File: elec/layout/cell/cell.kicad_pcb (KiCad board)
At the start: 4 copper layers, 65 parts

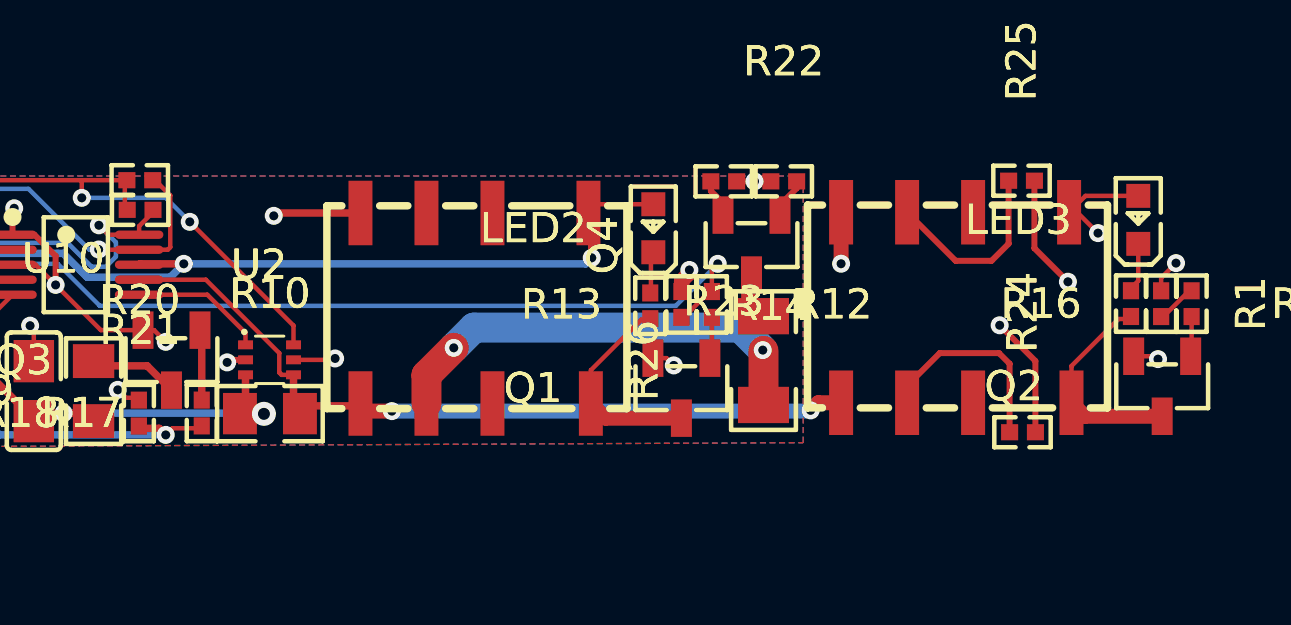
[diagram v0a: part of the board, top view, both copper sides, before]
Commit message: swap to relay with 20k in stock, through hole not smt
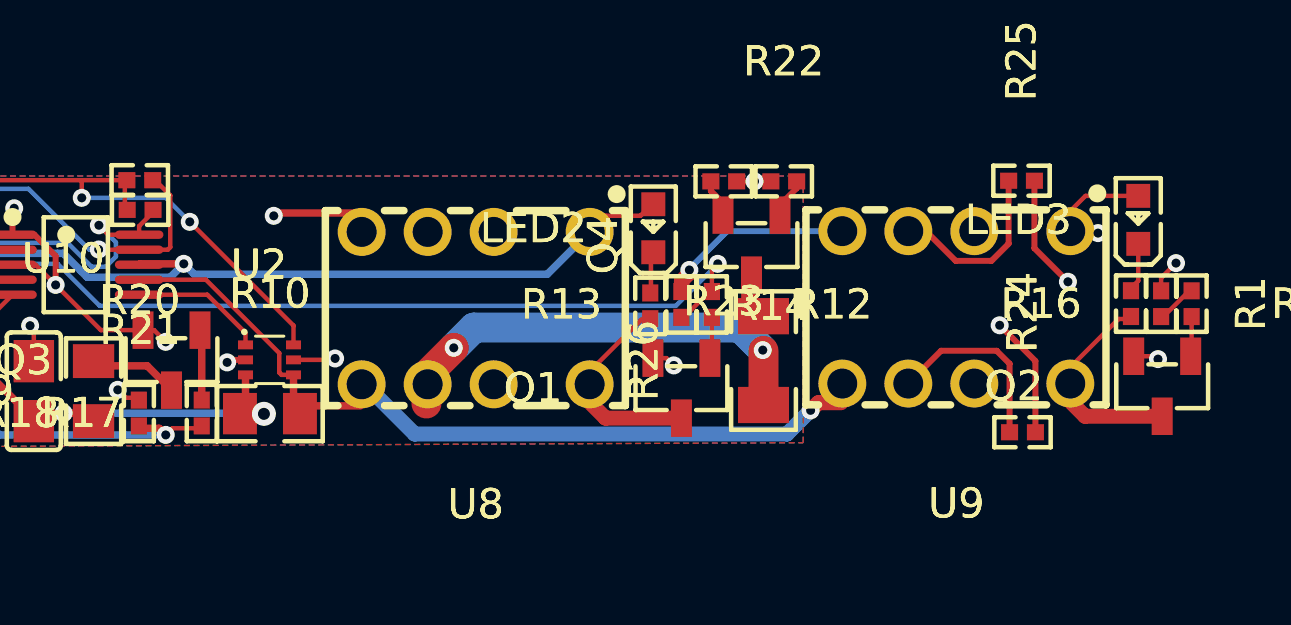
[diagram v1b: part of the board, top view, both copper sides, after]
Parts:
- U8, U9: footprint lib:RELAY-SMD_HFD4-5-SR -> atopile:RELAY-TH_HFDXXX-689a1e
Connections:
- C1 pad 1: hv-1 -> hv-10
- C1 pad 2: gnd-2 -> gnd
- C10 pad 1: hv-10 -> hv-6
- C10 pad 2: gnd -> gnd-8
- C11 pad 1: hv-10 -> hv-6
- C11 pad 2: gnd -> gnd-8
- C12 pad 1: hv-9 -> hv-7
- C12 pad 2: gnd -> gnd-8
- C13 pad 1: hv-4 -> hv-5
- C13 pad 2: gnd-7 -> gnd-4
- C14 pad 1: hv-4 -> hv-5
- C14 pad 2: gnd-7 -> gnd-4
- C15 pad 1: hv -> hv-9
- C15 pad 2: gnd -> gnd-8
- C16 pad 1: hv-6 -> hv-1
- C16 pad 2: gnd -> gnd-8
- C2 pad 1: hv -> hv-9
- C2 pad 2: gnd -> gnd-8
- C3 pad 1: hv -> hv-9
- C3 pad 2: gnd -> gnd-8
- C4 pad 1: hv -> hv-9
- C4 pad 2: gnd -> gnd-8
- C5 pad 1: hv -> hv-9
- C5 pad 2: gnd -> gnd-8
- C6 pad 1: hv-7 -> hv-4
- C6 pad 2: gnd -> gnd-8
- C7 pad 1: hv-7 -> hv-4
- C7 pad 2: gnd -> gnd-8
- C8 pad 1: hv-7 -> hv-4
- C8 pad 2: gnd -> gnd-8
- L1 pad 2: hv-7 -> hv-4
- L2 pad 1: hv-10 -> hv-6
- L2 pad 2: hv-9 -> hv-7
- LED1 pad 2: hv -> hv-9
- LED2 pad 2: hv -> hv-9
- LED3 pad 2: hv-4 -> hv-5
- Q1 pad 2: gnd -> gnd-8
- Q2 pad 2: gnd-7 -> gnd-4
- Q3 pad 2: gnd -> gnd-8
- Q3 pad 3: gnd-8 -> gnd-1
- Q4 pad 2: gnd-3 -> gnd-7
- Q4 pad 3: gnd-4 -> gnd-2
- R10 pad 1: hv-9 -> hv-7
- R10 pad 2: line-3 -> line-7
- R11 pad 2: gnd -> gnd-8
- R12 pad 1: line -> line-2
- R13 pad 1: line -> line-2
- R13 pad 2: gnd -> gnd-8
- R15 pad 1: line-7 -> line-11
- R16 pad 1: line-7 -> line-11
- R16 pad 2: gnd-7 -> gnd-4
- R17 pad 1: line-5 -> line-3
- R18 pad 1: line-5 -> line-3
- R18 pad 2: gnd -> gnd-8
- R19 pad 1: hv-9 -> hv-7
- R19 pad 2: gnd-8 -> gnd-1
- R20 pad 1: line-8 -> line
- R20 pad 2: hv-6 -> hv-1
- R21 pad 1: line-11 -> line-8
- R21 pad 2: hv-6 -> hv-1
- R22 pad 1: line-4 -> line-10
- R23 pad 1: line-4 -> line-10
- R23 pad 2: gnd-3 -> gnd-7
- R24 pad 1: hv-5 -> hv
- R24 pad 2: hv-3 -> hv-2
- R25 pad 1: gnd-6 -> gnd-5
- R25 pad 2: gnd-5 -> gnd-6
- R26 pad 2: gnd-4 -> gnd-2
- R3 pad 1: hv-7 -> hv-4
- R4 pad 2: gnd -> gnd-8
- R5 pad 1: line-14 -> line-1
- R7 pad 1: hv-10 -> hv-6
- R8 pad 2: gnd -> gnd-8
- R9 pad 1: line-2 -> line-6
- U1 pad 1: hv-1 -> hv-10
- U1 pad 2: gnd-2 -> gnd
- U1 pad 4: gnd -> gnd-8
- U1 pad 6: hv -> hv-9
- U10 pad 1: hv-6 -> hv-1
- U10 pad 10: gpio-net-1 -> gpio-net-2
- U10 pad 12: line-11 -> line-8
- U10 pad 13: line-8 -> line
- U10 pad 14: hv-6 -> hv-1
- U10 pad 15: hv-6 -> hv-1
- U10 pad 16: gnd -> gnd-8
- U10 pad 17: gnd -> gnd-8
- U10 pad 2: gpio-net-2 -> gpio-net-1
- U10 pad 4: line-14 -> line-1
- U10 pad 5: line-2 -> line-6
- U10 pad 6: gnd -> gnd-8
- U10 pad 7: line-5 -> line-3
- U10 pad 8: line -> line-2
- U10 pad 9: line-4 -> line-10
- U11 pad 1: hv-2 -> hv-3
- U11 pad 2: line-13 -> line-9
- U11 pad 3: line-12 -> line-13
- U11 pad 4: gnd-1 -> gnd-3
- U11 pad 5: gnd -> gnd-8
- U11 pad 6: line-11 -> line-8
- U11 pad 7: line-8 -> line
- U11 pad 8: hv-6 -> hv-1
- U12 pad 1: hv-4 -> hv-5
- U12 pad 2: line-10 -> line-14
- U12 pad 3: gnd-7 -> gnd-4
- U12 pad 4: line-6 -> line-4
- U13 pad 1: hv-4 -> hv-5
- U13 pad 2: line-6 -> line-4
- U13 pad 3: gnd-7 -> gnd-4
- U13 pad 4: line-1 -> line-5
- U14 pad 1: gnd -> gnd-8
- U14 pad 2: hv-6 -> hv-1
- U14 pad 3: hv -> hv-9
- U2 pad 1: gnd -> gnd-8
- U2 pad 10: line-11 -> line-8
- U2 pad 3: gnd -> gnd-8
- U2 pad 4: hv-7 -> hv-4
- U2 pad 5: hv-10 -> hv-6
- U2 pad 6: line-9 -> line-12
- U2 pad 7: line-3 -> line-7
- U2 pad 8: hv -> hv-9
- U2 pad 9: line-8 -> line
- U3 pad 2: gnd -> gnd-8
- U3 pad 3: hv-6 -> hv-1
- U3 pad 4: line-8 -> line
- U3 pad 5: line-11 -> line-8
- U3 pad 6: hv -> hv-9
- U4 pad 1: gnd -> gnd-8
- U4 pad 3: hv -> hv-9
- U5 pad 2: gnd -> gnd-8
- U5 pad 3: hv-6 -> hv-1
- U5 pad 4: line-8 -> line
- U5 pad 5: line-11 -> line-8
- U5 pad 6: gnd -> gnd-8
- U6 pad 1: hv-10 -> hv-6
- U6 pad 3: gnd -> gnd-8
- U6 pad 6: hv-7 -> hv-4
- U6 pad 7: gnd -> gnd-8
- U7 pad 1: line-9 -> line-12
- U7 pad 2: gnd -> gnd-8
- U7 pad 3: hv-9 -> hv-7
- U7 pad 4: line-3 -> line-7
- U7 pad 5: gnd -> gnd-8
- U7 pad 6: hv-6 -> hv-1
- U8 pad 1: hv -> hv-9
- U8 pad 2: (no net) -> output_relay.relay.footprint.pins[1].net-net
- U8 pad 3: gnd-3 -> gnd-7
- U8 pad 4: gnd -> gnd-8
- U8 pad 5: line-3 -> line-7
- U8 pad 7: (no net) -> output_relay.relay.footprint.pins[6].net-net
- U9 pad 1: hv-4 -> hv-5
- U9 pad 2: (no net) -> dmm_relay.relay.footprint.pins[1].net-net
- U9 pad 3: gnd-6 -> gnd-5
- U9 pad 4: gnd -> gnd-8
- U9 pad 5: line-3 -> line-7
- U9 pad 6: hv-5 -> hv
- U9 pad 7: (no net) -> dmm_relay.relay.footprint.pins[6].net-net
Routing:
- net gnd-8: track 3.42 -> 110.0 mm, vias 0 -> 31
- net gnd: track 106.1 -> 10.8 mm, vias 32 -> 1
- net hv: track 75.3 -> 6.35 mm, vias 4 -> 0
- net hv-9: track 13.2 -> 74.7 mm, vias 2 -> 3
- net line-11: track 43.5 -> 1.44 mm, vias 5 -> 0
- net line-10: track 0.00 -> 30.5 mm, vias 0 -> 2
- net hv-1: track 4.33 -> 34.0 mm, vias 0 -> 8
- net line-4: track 30.5 -> 2.29 mm, vias 2 -> 0
- net line-7: track 1.44 -> 27.5 mm, vias 0 -> 1
- net line-2: track 7.72 -> 30.4 mm
- net hv-6: track 34.0 -> 15.6 mm, vias 8 -> 0
- net line: track 30.4 -> 44.5 mm, vias 2 -> 4
- net line-5: track 13.5 -> 0.00 mm, vias 2 -> 0
- net line-3: track 26.6 -> 13.5 mm
- net line-14: track 12.8 -> 0.00 mm, vias 2 -> 0
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- added copper zone on B.Cu, net gnd-8
- added copper zone on F.Cu, net gnd-8
- added copper zone on In2.Cu, net gnd-8
- added copper zone on In1.Cu, net hv-1
- removed copper zone on B.Cu, net gnd
- removed copper zone on F.Cu, net gnd
- removed copper zone on In2.Cu, net gnd
- removed copper zone on In1.Cu, net hv-6

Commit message: Cleanup layout
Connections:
- C1 pad 1: hv-10 -> hv-9
- C10 pad 1: hv-6 -> hv-4
- C10 pad 2: gnd-8 -> gnd-7
- C11 pad 1: hv-6 -> hv-4
- C11 pad 2: gnd-8 -> gnd-7
- C12 pad 1: hv-7 -> hv-1
- C12 pad 2: gnd-8 -> gnd-7
- C13 pad 1: hv-5 -> hv-7
- C13 pad 2: gnd-4 -> gnd-1
- C14 pad 1: hv-5 -> hv-7
- C14 pad 2: gnd-4 -> gnd-1
- C15 pad 1: hv-9 -> hv-3
- C15 pad 2: gnd-8 -> gnd-7
- C16 pad 1: hv-1 -> hv-5
- C16 pad 2: gnd-8 -> gnd-7
- C2 pad 1: hv-9 -> hv-3
- C2 pad 2: gnd-8 -> gnd-7
- C3 pad 1: hv-9 -> hv-3
- C3 pad 2: gnd-8 -> gnd-7
- C4 pad 1: hv-9 -> hv-3
- C4 pad 2: gnd-8 -> gnd-7
- C5 pad 1: hv-9 -> hv-3
- C5 pad 2: gnd-8 -> gnd-7
- C6 pad 1: hv-4 -> hv-10
- C6 pad 2: gnd-8 -> gnd-7
- C7 pad 1: hv-4 -> hv-10
- C7 pad 2: gnd-8 -> gnd-7
- C8 pad 1: hv-4 -> hv-10
- C8 pad 2: gnd-8 -> gnd-7
- L1 pad 2: hv-4 -> hv-10
- L2 pad 1: hv-6 -> hv-4
- L2 pad 2: hv-7 -> hv-1
- LED1 pad 2: hv-9 -> hv-3
- LED2 pad 2: hv-9 -> hv-3
- LED3 pad 2: hv-5 -> hv-7
- Q1 pad 2: gnd-8 -> gnd-7
- Q2 pad 2: gnd-4 -> gnd-1
- Q3 pad 2: gnd-8 -> gnd-7
- Q3 pad 3: gnd-1 -> gnd-4
- Q4 pad 2: gnd-7 -> gnd-6
- Q4 pad 3: gnd-2 -> gnd-3
- R10 pad 1: hv-7 -> hv-1
- R10 pad 2: line-7 -> line-10
- R11 pad 2: gnd-8 -> gnd-7
- R12 pad 1: line-2 -> line-12
- R13 pad 1: line-2 -> line-12
- R13 pad 2: gnd-8 -> gnd-7
- R15 pad 1: line-11 -> line-3
- R16 pad 1: line-11 -> line-3
- R16 pad 2: gnd-4 -> gnd-1
- R17 pad 1: line-3 -> line-1
- R18 pad 1: line-3 -> line-1
- R18 pad 2: gnd-8 -> gnd-7
- R19 pad 1: hv-7 -> hv-1
- R19 pad 2: gnd-1 -> gnd-4
- R20 pad 1: line -> line-8
- R20 pad 2: hv-1 -> hv-5
- R21 pad 1: line-8 -> line-11
- R21 pad 2: hv-1 -> hv-5
- R22 pad 1: line-10 -> line-5
- R23 pad 1: line-10 -> line-5
- R23 pad 2: gnd-7 -> gnd-6
- R24 pad 1: hv -> hv-2
- R24 pad 2: hv-2 -> hv
- R25 pad 1: gnd-5 -> gnd-2
- R25 pad 2: gnd-6 -> gnd-5
- R26 pad 2: gnd-2 -> gnd-3
- R3 pad 1: hv-4 -> hv-10
- R4 pad 2: gnd-8 -> gnd-7
- R5 pad 1: line-1 -> line-13
- R7 pad 1: hv-6 -> hv-4
- R8 pad 2: gnd-8 -> gnd-7
- R9 pad 1: line-6 -> line-4
- U1 pad 1: hv-10 -> hv-9
- U1 pad 4: gnd-8 -> gnd-7
- U1 pad 6: hv-9 -> hv-3
- U10 pad 1: hv-1 -> hv-5
- U10 pad 10: gpio-net-2 -> gpio-net-1
- U10 pad 12: line-8 -> line-11
- U10 pad 13: line -> line-8
- U10 pad 14: hv-1 -> hv-5
- U10 pad 15: hv-1 -> hv-5
- U10 pad 16: gnd-8 -> gnd-7
- U10 pad 17: gnd-8 -> gnd-7
- U10 pad 2: gpio-net-1 -> gpio-net
- U10 pad 3: gpio-net -> gpio-net-2
- U10 pad 4: line-1 -> line-13
- U10 pad 5: line-6 -> line-4
- U10 pad 6: gnd-8 -> gnd-7
- U10 pad 7: line-3 -> line-1
- U10 pad 8: line-2 -> line-12
- U10 pad 9: line-10 -> line-5
- U11 pad 1: hv-3 -> hv-6
- U11 pad 2: line-9 -> line-2
- U11 pad 3: line-13 -> line-14
- U11 pad 4: gnd-3 -> gnd-8
- U11 pad 5: gnd-8 -> gnd-7
- U11 pad 6: line-8 -> line-11
- U11 pad 7: line -> line-8
- U11 pad 8: hv-1 -> hv-5
- U12 pad 1: hv-5 -> hv-7
- U12 pad 2: line-14 -> line-6
- U12 pad 3: gnd-4 -> gnd-1
- U12 pad 4: line-4 -> line
- U13 pad 1: hv-5 -> hv-7
- U13 pad 2: line-4 -> line
- U13 pad 3: gnd-4 -> gnd-1
- U13 pad 4: line-5 -> line-7
- U14 pad 1: gnd-8 -> gnd-7
- U14 pad 2: hv-1 -> hv-5
- U14 pad 3: hv-9 -> hv-3
- U2 pad 1: gnd-8 -> gnd-7
- U2 pad 10: line-8 -> line-11
- U2 pad 3: gnd-8 -> gnd-7
- U2 pad 4: hv-4 -> hv-10
- U2 pad 5: hv-6 -> hv-4
- U2 pad 6: line-12 -> line-9
- U2 pad 7: line-7 -> line-10
- U2 pad 8: hv-9 -> hv-3
- U2 pad 9: line -> line-8
- U3 pad 2: gnd-8 -> gnd-7
- U3 pad 3: hv-1 -> hv-5
- U3 pad 4: line -> line-8
- U3 pad 5: line-8 -> line-11
- U3 pad 6: hv-9 -> hv-3
- U4 pad 1: gnd-8 -> gnd-7
- U4 pad 3: hv-9 -> hv-3
- U5 pad 2: gnd-8 -> gnd-7
- U5 pad 3: hv-1 -> hv-5
- U5 pad 4: line -> line-8
- U5 pad 5: line-8 -> line-11
- U5 pad 6: gnd-8 -> gnd-7
- U6 pad 1: hv-6 -> hv-4
- U6 pad 3: gnd-8 -> gnd-7
- U6 pad 6: hv-4 -> hv-10
- U6 pad 7: gnd-8 -> gnd-7
- U7 pad 1: line-12 -> line-9
- U7 pad 2: gnd-8 -> gnd-7
- U7 pad 3: hv-7 -> hv-1
- U7 pad 4: line-7 -> line-10
- U7 pad 5: gnd-8 -> gnd-7
- U7 pad 6: hv-1 -> hv-5
- U8 pad 1: hv-9 -> hv-3
- U8 pad 3: gnd-7 -> gnd-6
- U8 pad 4: gnd-8 -> gnd-7
- U8 pad 5: line-7 -> line-10
- U9 pad 1: hv-5 -> hv-7
- U9 pad 3: gnd-5 -> gnd-2
- U9 pad 4: gnd-8 -> gnd-7
- U9 pad 5: line-7 -> line-10
- U9 pad 6: hv -> hv-2
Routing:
- net gnd-8: track 110.0 -> 0.00 mm, vias 31 -> 0
- net gnd-7: track 1.30 -> 110.0 mm, vias 0 -> 31
- net hv-3: track 0.00 -> 74.7 mm, vias 0 -> 3
- net hv-9: track 74.7 -> 4.33 mm, vias 3 -> 0
- net line: track 44.5 -> 2.29 mm, vias 4 -> 0
- net line-11: track 1.44 -> 43.5 mm, vias 0 -> 5
- net line-5: track 0.00 -> 30.5 mm, vias 0 -> 2
- net line-2: track 30.4 -> 0.00 mm, vias 2 -> 0
- net line-7: track 27.5 -> 0.00 mm, vias 1 -> 0
- net line-12: track 4.47 -> 30.4 mm, vias 0 -> 2
- net hv-5: track 11.6 -> 34.0 mm, vias 2 -> 8
- net hv-1: track 34.0 -> 13.2 mm, vias 8 -> 2
- net hv-10: track 4.33 -> 24.3 mm, vias 0 -> 2
- net hv-6: track 15.6 -> 0.00 mm
- net line-13: track 0.00 -> 12.8 mm, vias 0 -> 2
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- added copper zone on B.Cu, net gnd-7
- added copper zone on F.Cu, net gnd-7
- added copper zone on In2.Cu, net gnd-7
- added copper zone on In1.Cu, net hv-5
- removed copper zone on B.Cu, net gnd-8
- removed copper zone on F.Cu, net gnd-8
- removed copper zone on In2.Cu, net gnd-8
- removed copper zone on In1.Cu, net hv-1

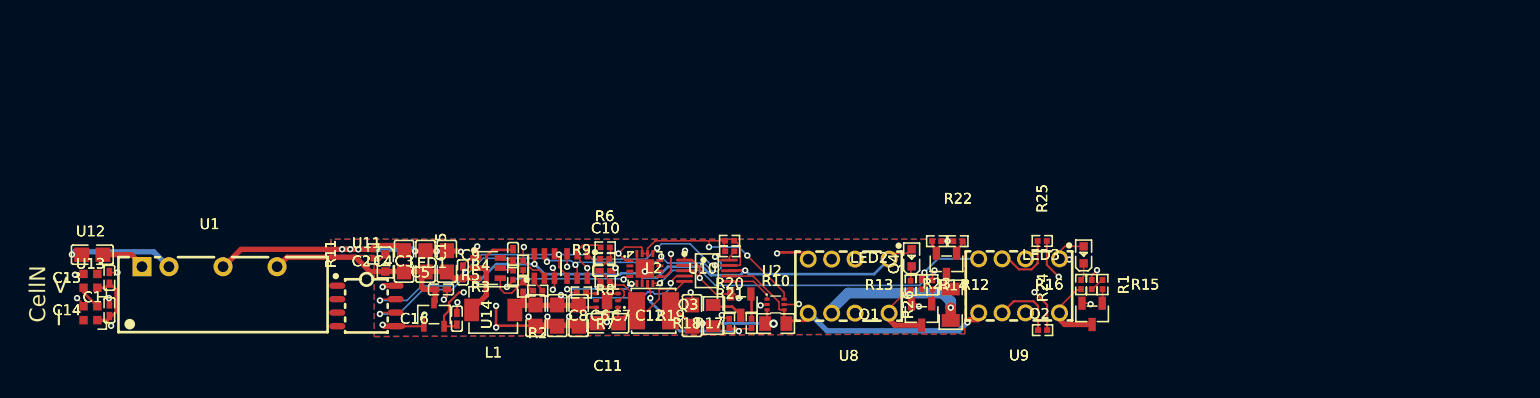
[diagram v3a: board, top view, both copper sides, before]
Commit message: update n-fet part for stock
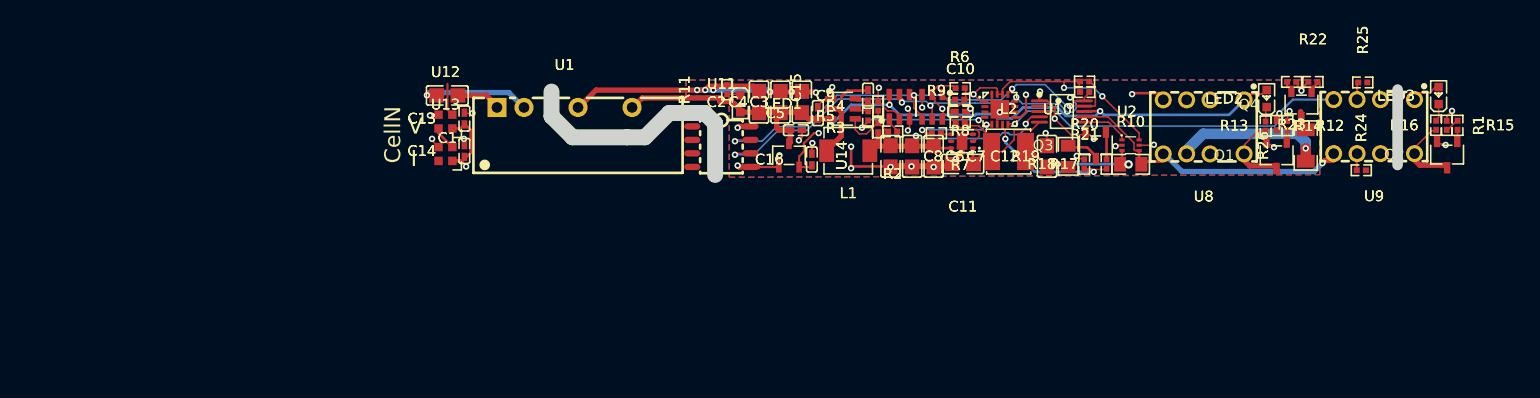
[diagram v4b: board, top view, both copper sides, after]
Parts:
- Q1, Q2, Q3, Q4: footprint atopile:SOT-23-3_L2.9-W1.3-P1.90-LS2.4-BR-688f29 -> atopile:SOT-23-3_L2.9-W1.6-P1.90-LS2.8-BR-186170
- moved R11 36.7 mm to (117.5, 101.8)
- moved C7 36.6 mm to (136.9, 108.0)
- moved R3 36.6 mm to (131.7, 105.3)
- moved C10 36.6 mm to (139.4, 103.8)
- moved C11 36.6 mm to (139.7, 108.7)
- moved C14 36.6 mm to (92.8, 107.5)
- moved C15 36.6 mm to (124.0, 105.6)
- moved C16 36.6 mm to (125.5, 108.3)
- moved C3 36.6 mm to (124.5, 102.9)
- moved C4 36.6 mm to (122.5, 102.9)
- moved C5 36.6 mm to (126.0, 104.0)
- moved C6 36.6 mm to (134.9, 108.0)
- moved C8 36.6 mm to (132.9, 108.0)
- moved Q1 36.6 mm to (169.2, 107.9)
- moved Q4 36.6 mm to (171.5, 103.2)
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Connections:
- C1 pad 1: hv-9 -> hv
- C1 pad 2: gnd -> gnd-8
- C10 pad 1: hv-4 -> hv-9
- C10 pad 2: gnd-7 -> gnd
- C11 pad 1: hv-4 -> hv-9
- C11 pad 2: gnd-7 -> gnd
- C12 pad 1: hv-1 -> hv-5
- C12 pad 2: gnd-7 -> gnd
- C13 pad 1: hv-7 -> hv-2
- C13 pad 2: gnd-1 -> gnd-5
- C14 pad 1: hv-7 -> hv-2
- C14 pad 2: gnd-1 -> gnd-5
- C15 pad 1: hv-3 -> 5V
- C15 pad 2: gnd-7 -> gnd
- C16 pad 1: hv-5 -> 3V3
- C16 pad 2: gnd-7 -> gnd
- C2 pad 1: hv-3 -> 5V
- C2 pad 2: gnd-7 -> gnd
- C3 pad 1: hv-3 -> 5V
- C3 pad 2: gnd-7 -> gnd
- C4 pad 1: hv-3 -> 5V
- C4 pad 2: gnd-7 -> gnd
- C5 pad 1: hv-3 -> 5V
- C5 pad 2: gnd-7 -> gnd
- C6 pad 1: hv-10 -> hv-7
- C6 pad 2: gnd-7 -> gnd
- C7 pad 1: hv-10 -> hv-7
- C7 pad 2: gnd-7 -> gnd
- C8 pad 1: hv-10 -> hv-7
- C8 pad 2: gnd-7 -> gnd
- L1 pad 2: hv-10 -> hv-7
- L2 pad 1: hv-4 -> hv-9
- L2 pad 2: hv-1 -> hv-5
- LED1 pad 2: hv-3 -> 5V
- LED2 pad 2: hv-3 -> 5V
- LED3 pad 2: hv-7 -> hv-2
- Q1 pad 2: gnd-7 -> gnd
- Q2 pad 2: gnd-1 -> gnd-5
- Q3 pad 2: gnd-7 -> gnd
- Q3 pad 3: gnd-4 -> gnd-2
- Q4 pad 2: gnd-6 -> gnd-7
- Q4 pad 3: gnd-3 -> gnd-1
- R10 pad 1: hv-1 -> hv-5
- R10 pad 2: line-10 -> hv-8
- R11 pad 2: gnd-7 -> gnd
- R12 pad 1: line-12 -> line-4
- R13 pad 1: line-12 -> line-4
- R13 pad 2: gnd-7 -> gnd
- R15 pad 1: line-3 -> line-7
- R16 pad 1: line-3 -> line-7
- R16 pad 2: gnd-1 -> gnd-5
- R17 pad 1: line-1 -> line-11
- R18 pad 1: line-1 -> line-11
- R18 pad 2: gnd-7 -> gnd
- R19 pad 1: hv-1 -> hv-5
- R19 pad 2: gnd-4 -> gnd-2
- R20 pad 1: line-8 -> line-6
- R20 pad 2: hv-5 -> 3V3
- R21 pad 1: line-11 -> line-10
- R21 pad 2: hv-5 -> 3V3
- R22 pad 1: line-5 -> line-1
- R23 pad 1: line-5 -> line-1
- R23 pad 2: gnd-6 -> gnd-7
- R24 pad 1: hv-2 -> hv-6
- R24 pad 2: hv -> hv-4
- R25 pad 1: gnd-2 -> gnd-6
- R25 pad 2: gnd-5 -> gnd-3
- R26 pad 1: hv-8 -> hv-3
- R26 pad 2: gnd-3 -> gnd-1
- R3 pad 1: hv-10 -> hv-7
- R4 pad 2: gnd-7 -> gnd
- R5 pad 1: line-13 -> line-5
- R7 pad 1: hv-4 -> hv-9
- R8 pad 2: gnd-7 -> gnd
- R9 pad 1: line-4 -> line-2
- U1 pad 1: hv-9 -> hv
- U1 pad 2: gnd -> gnd-8
- U1 pad 4: gnd-7 -> gnd
- U1 pad 6: hv-3 -> 5V
- U10 pad 1: hv-5 -> 3V3
- U10 pad 10: gpio-net-1 -> gpio-net-2
- U10 pad 12: line-11 -> line-10
- U10 pad 13: line-8 -> line-6
- U10 pad 14: hv-5 -> 3V3
- U10 pad 15: hv-5 -> 3V3
- U10 pad 16: gnd-7 -> gnd
- U10 pad 17: gnd-7 -> gnd
- U10 pad 3: gpio-net-2 -> gpio-net-1
- U10 pad 4: line-13 -> line-5
- U10 pad 5: line-4 -> line-2
- U10 pad 6: gnd-7 -> gnd
- U10 pad 7: line-1 -> line-11
- U10 pad 8: line-12 -> line-4
- U10 pad 9: line-5 -> line-1
- U11 pad 1: hv-6 -> hv-1
- U11 pad 2: line-2 -> line-3
- U11 pad 3: line-14 -> line-8
- U11 pad 4: gnd-8 -> gnd-4
- U11 pad 5: gnd-7 -> gnd
- U11 pad 6: line-11 -> line-10
- U11 pad 7: line-8 -> line-6
- U11 pad 8: hv-5 -> 3V3
- U12 pad 1: hv-7 -> hv-2
- U12 pad 2: line-6 -> DOUT
- U12 pad 3: gnd-1 -> gnd-5
- U12 pad 4: line -> line-9
- U13 pad 1: hv-7 -> hv-2
- U13 pad 2: line -> line-9
- U13 pad 3: gnd-1 -> gnd-5
- U13 pad 4: line-7 -> DIN
- U14 pad 1: gnd-7 -> gnd
- U14 pad 2: hv-5 -> 3V3
- U14 pad 3: hv-3 -> 5V
- U2 pad 1: gnd-7 -> gnd
- U2 pad 10: line-11 -> line-10
- U2 pad 3: gnd-7 -> gnd
- U2 pad 4: hv-10 -> hv-7
- U2 pad 5: hv-4 -> hv-9
- U2 pad 6: line-9 -> line
- U2 pad 7: line-10 -> hv-8
- U2 pad 8: hv-3 -> 5V
- U2 pad 9: line-8 -> line-6
- U3 pad 2: gnd-7 -> gnd
- U3 pad 3: hv-5 -> 3V3
- U3 pad 4: line-8 -> line-6
- U3 pad 5: line-11 -> line-10
- U3 pad 6: hv-3 -> 5V
- U4 pad 1: gnd-7 -> gnd
- U4 pad 3: hv-3 -> 5V
- U5 pad 2: gnd-7 -> gnd
- U5 pad 3: hv-5 -> 3V3
- U5 pad 4: line-8 -> line-6
- U5 pad 5: line-11 -> line-10
- U5 pad 6: gnd-7 -> gnd
- U6 pad 1: hv-4 -> hv-9
- U6 pad 3: gnd-7 -> gnd
- U6 pad 6: hv-10 -> hv-7
- U6 pad 7: gnd-7 -> gnd
- U7 pad 1: line-9 -> line
- U7 pad 2: gnd-7 -> gnd
- U7 pad 3: hv-1 -> hv-5
- U7 pad 4: line-10 -> hv-8
- U7 pad 5: gnd-7 -> gnd
- U7 pad 6: hv-5 -> 3V3
- U8 pad 1: hv-3 -> 5V
- U8 pad 3: gnd-6 -> gnd-7
- U8 pad 4: gnd-7 -> gnd
- U8 pad 5: line-10 -> hv-8
- U8 pad 6: hv-8 -> hv-3
- U9 pad 1: hv-7 -> hv-2
- U9 pad 3: gnd-2 -> gnd-6
- U9 pad 4: gnd-7 -> gnd
- U9 pad 5: line-10 -> hv-8
- U9 pad 6: hv-2 -> hv-6
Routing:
- net gnd-7: track 110.0 -> 1.30 mm, vias 31 -> 0
- net gnd: track 10.8 -> 105.5 mm, vias 1 -> 31
- net 5V: track 0.00 -> 75.2 mm, vias 0 -> 3
- net hv-3: track 74.7 -> 14.3 mm, vias 3 -> 1
- net line-8: track 44.5 -> 0.00 mm, vias 4 -> 0
- net line-6: track 0.00 -> 44.5 mm, vias 0 -> 4
- net 3V3: track 0.00 -> 34.0 mm, vias 0 -> 8
- net line-12: track 30.4 -> 0.00 mm, vias 2 -> 0
- net line-11: track 43.5 -> 13.5 mm, vias 5 -> 2
- net hv-10: track 24.3 -> 0.00 mm, vias 2 -> 0
- net line-4: track 7.72 -> 30.4 mm
- net hv-5: track 34.0 -> 13.2 mm, vias 8 -> 2
- net line-1: track 13.5 -> 31.7 mm
- net line-5: track 30.5 -> 12.8 mm
- net line-10: track 27.5 -> 43.5 mm, vias 1 -> 5
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- added copper zone on In1.Cu, net 3V3
- added copper zone on B.Cu, net gnd
- added copper zone on F.Cu, net gnd
- added copper zone on In2.Cu, net gnd
- removed copper zone on B.Cu, net gnd-7
- removed copper zone on F.Cu, net gnd-7
- removed copper zone on In2.Cu, net gnd-7
- removed copper zone on In1.Cu, net hv-5
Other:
- board outline added: 79.5 x 8 mm
